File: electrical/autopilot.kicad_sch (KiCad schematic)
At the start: 9 parts

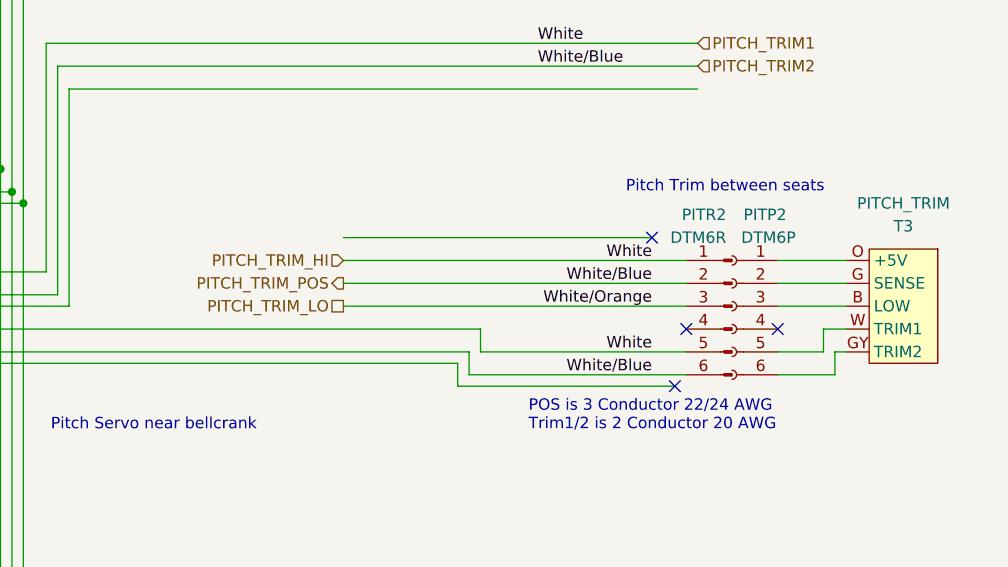
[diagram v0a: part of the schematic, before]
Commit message: Fixed trim POS.
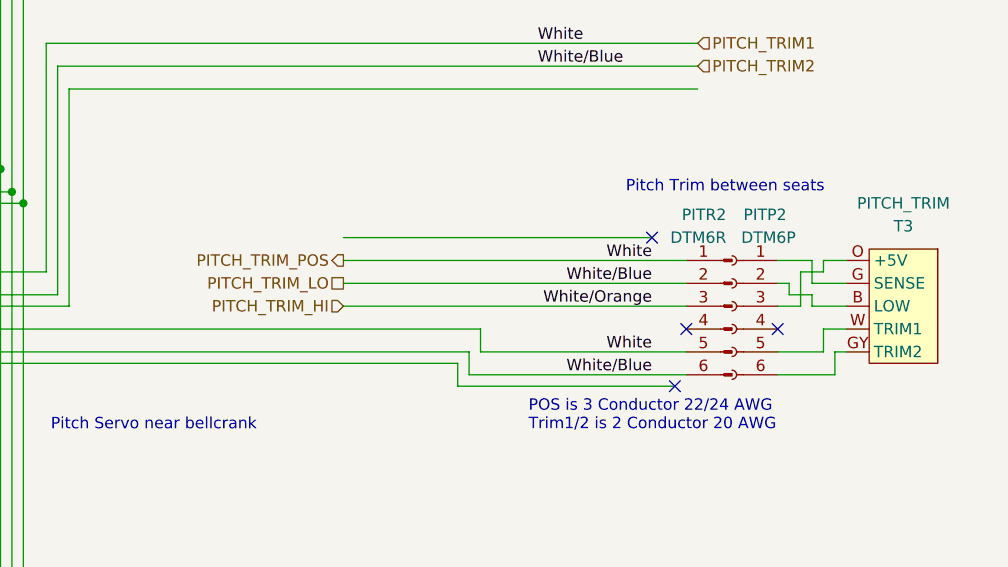
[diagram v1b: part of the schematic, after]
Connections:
- net at PITCH_TRIM.B (LOW): now also PITP2.2 (Pin_2); no longer PITP2.3 (Pin_3)
- net at PITCH_TRIM.G (SENSE): now also PITP2.1 (Pin_1); no longer PITP2.2 (Pin_2)
- net at PITCH_TRIM.O (+5V): now also PITP2.3 (Pin_3); no longer PITP2.1 (Pin_1)
- net PITCH_TRIM_LO renamed PITCH_TRIM_HI
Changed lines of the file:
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@@
+	(wire
+		(pts
+			(xy 158.75 105.41) (xy 158.75 106.68)
+		)
+		(stroke
+			(width 0)
+			(type default)
+		)
+	)
 	(wire
 		(pts
@@
 	(wire
 		(pts
-			(xy 157.48 102.87) (xy 165.1 102.87)
-		)
-		(stroke
-			(width 0)
-			(type default)
-		)
-	)
-	(wire
-		(pts
 			(xy 68.58 53.34) (xy 91.44 53.34)
 		)
@@
 	(wire
 		(pts
+			(xy 158.75 106.68) (xy 161.29 106.68)
+		)
+		(stroke
+			(width 0)
+			(type default)
+		)
+	)
+	(wire
+		(pts
+			(xy 161.29 102.87) (xy 157.48 102.87)
+		)
+		(stroke
+			(width 0)
+			(type default)
+		)
+	)
+	(wire
+		(pts
 			(xy 60.96 186.69) (xy 55.88 186.69)
 		)
@@
 	(wire
 		(pts
+			(xy 157.48 105.41) (xy 158.75 105.41)
+		)
+		(stroke
+			(width 0)
+			(type default)
+		)
+	)
+	(wire
+		(pts
 			(xy 163.83 113.03) (xy 165.1 113.03)
 		)
@@
 	(wire
 		(pts
+			(xy 160.02 107.95) (xy 160.02 104.14)
+		)
+		(stroke
+			(width 0)
+			(type default)
+		)
+	)
+	(wire
+		(pts
 			(xy 177.8 41.91) (xy 203.2 41.91)
 		)
@@
 	(wire
 		(pts
-			(xy 157.48 105.41) (xy 165.1 105.41)
-		)
-		(stroke
-			(width 0)
-			(type default)
-		)
-	)
-	(wire
-		(pts
 			(xy 76.2 78.74) (xy 148.59 78.74)
 		)
@@
 	(wire
 		(pts
+			(xy 161.29 106.68) (xy 161.29 107.95)
+		)
+		(stroke
+			(width 0)
+			(type default)
+		)
+	)
+	(wire
+		(pts
 			(xy 55.88 22.86) (xy 64.77 22.86)
 		)
@@
 	(wire
 		(pts
-			(xy 157.48 107.95) (xy 165.1 107.95)
-		)
-		(stroke
-			(width 0)
-			(type default)
-		)
-	)
-	(wire
-		(pts
 			(xy 78.74 83.82) (xy 78.74 107.95)
 		)
@@
 	(wire
 		(pts
+			(xy 161.29 105.41) (xy 161.29 102.87)
+		)
+		(stroke
+			(width 0)
+			(type default)
+		)
+	)
+	(wire
+		(pts
 			(xy 55.88 184.15) (xy 60.96 184.15)
 		)
@@
 	(wire
 		(pts
+			(xy 157.48 107.95) (xy 160.02 107.95)
+		)
+		(stroke
+			(width 0)
+			(type default)
+		)
+	)
+	(wire
+		(pts
 			(xy 196.85 33.02) (xy 200.66 33.02)
 		)
@@
 	(wire
 		(pts
+			(xy 165.1 105.41) (xy 161.29 105.41)
+		)
+		(stroke
+			(width 0)
+			(type default)
+		)
+	)
+	(wire
+		(pts
 			(xy 68.58 116.84) (xy 68.58 53.34)
 		)
@@
 	(wire
 		(pts
+			(xy 161.29 107.95) (xy 165.1 107.95)
+		)
+		(stroke
+			(width 0)
+			(type default)
+		)
+	)
+	(wire
+		(pts
 			(xy 193.04 29.21) (xy 204.47 29.21)
 		)
@@
 	(wire
 		(pts
+			(xy 160.02 104.14) (xy 162.56 104.14)
+		)
+		(stroke
+			(width 0)
+			(type default)
+		)
+	)
+	(wire
+		(pts
 			(xy 73.66 33.02) (xy 76.2 33.02)
 		)
@@
 	(wire
 		(pts
+			(xy 162.56 104.14) (xy 162.56 102.87)
+		)
+		(stroke
+			(width 0)
+			(type default)
+		)
+	)
+	(wire
+		(pts
 			(xy 162.56 113.03) (xy 162.56 110.49)
 		)
@@
 		(pts
 			(xy 55.88 120.65) (xy 58.42 120.65)
+		)
+		(stroke
+			(width 0)
+			(type default)
+		)
+	)
+	(wire
+		(pts
+			(xy 162.56 102.87) (xy 165.1 102.87)
 		)
 		(stroke
@@
 	(hierarchical_label "PITCH_TRIM_LO"
 		(shape passive)
-		(at 109.22 107.95 180)
-		(effects
-			(font
-				(size 1.27 1.27)
-			)
-			(justify right)
-		)
-	)
-	(hierarchical_label "PITCH_TRIM_POS"
-		(shape output)
 		(at 109.22 105.41 180)
 		(effects
@@
 	(hierarchical_label "PITCH_TRIM_HI"
 		(shape input)
-		(at 109.22 102.87 180)
+		(at 109.22 107.95 180)
 		(effects
 			(font
@@
 		(effects
 			(font
+				(size 1.27 1.27)
+			)
+			(justify right)
+		)
+	)
+	(hierarchical_label "PITCH_TRIM_POS"
+		(shape output)
+		(at 109.22 102.87 180)
+		(effects
+			(font
